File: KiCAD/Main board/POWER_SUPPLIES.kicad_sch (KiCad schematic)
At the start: 32 parts, among them U18 12V, U19 5V, U20 8V, U21 15V, U23 LIN_REG_±5V, U24 LIN_REG_±12V, U28 12V, U29 AP2111H-3.3TRG1, U31 AP2111H-3.3TRG1, U9 SEPIC_-15V_LT3579

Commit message: Main board
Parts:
- added TP17: TestPoint, TestPoint:TestPoint_Pad_D2.0mm, symbol Connector:TestPoint
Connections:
- net -15VD1: now reaches U23.6 (-VIN), U23.6 (-VIN), U24.6 (-VIN), U24.6 (-VIN), U9.3 (VOUT)
- net -15VD1: now also TP17.1
- net +15VD1: now reaches TP11.1, U21.1 (VOUT), U24.1 (+VIN), U24.1 (+VIN)
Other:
- moved on the sheet: C2, TP10, TP15, TP16, TP2, TP3, TP4, TP5, TP6, TP7, TP8, U23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

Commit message: Worked on main board schematic
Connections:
- net +12VD1: now also U28.2 (VOUT)
- net +15VD1: now also U21.2 (VOUT)
- net +5VD1: now also U19.2 (VOUT)
- net DC_POWER_IN: now also U18.5 (VIN), U19.5 (VIN), U20.5 (VIN), U21.5 (VIN), U28.5 (VIN); no longer U18.3 (VIN), U19.3 (VIN), U20.3 (VIN), U21.3 (VIN), U28.3 (VIN)
- net GND: now also U18.3 (GND), U18.4 (GND), U19.3 (GND), U19.4 (GND), U20.3 (GND), U20.4 (GND), U21.3 (GND), U21.4 (GND), U28.3 (GND), U28.4 (GND); no longer U18.2 (GND), U19.2 (GND), U20.2 (GND), U21.2 (GND), U28.2 (GND)
- net at TP9.1, U20.1 (VOUT), U23.1 (+VIN)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: now also U20.2 (VOUT)
- net at TP12.1, U18.1 (VOUT), U9.1 (VIN): now also U18.2 (VOUT)
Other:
- moved on the sheet: C2, TP1, TP10, TP11, TP12, TP13, TP15, TP16, TP17, TP2, TP3, TP4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

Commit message: Ad good as finilized the main board schematic
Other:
- note removed: "Check all regulator symbols and footprints with someone else"
- title: (none) -> AUDIO-DSP_MAIN_BOARD
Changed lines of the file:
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@@
 (kicad_sch (version 20230121) (generator eeschema)
   (paper "A4")
+  (title_block
+    (title "AUDIO-DSP_MAIN_BOARD")
+    (rev "R01")
+  )
   (junction (at 125.73 173.99) (diameter 0) (color 0 0 0 0)
   )
@@
   )
   (rectangle (start 93.98 35.56) (end 147.32 191.77)
-    (stroke (width 0) (type dash))
+    (stroke (width 0) (type dash) (color 100 100 100 1))
     (fill (type none))
   )
   (rectangle (start 13.97 13.97) (end 92.71 163.83)
-    (stroke (width 0) (type dash))
+    (stroke (width 0) (type dash) (color 100 100 100 1))
     (fill (type none))
   )
-  (text "Check all regulator symbols and footprints with someone else"
-    (at 93.98 34.29 0)
-    (effects (font (size 1.27 1.27) (color 200 0 200 1)) (justify left bottom))
-  )
   (text "Add thermal pad to pin 4 for cooling" (at 116.84 189.23 0)

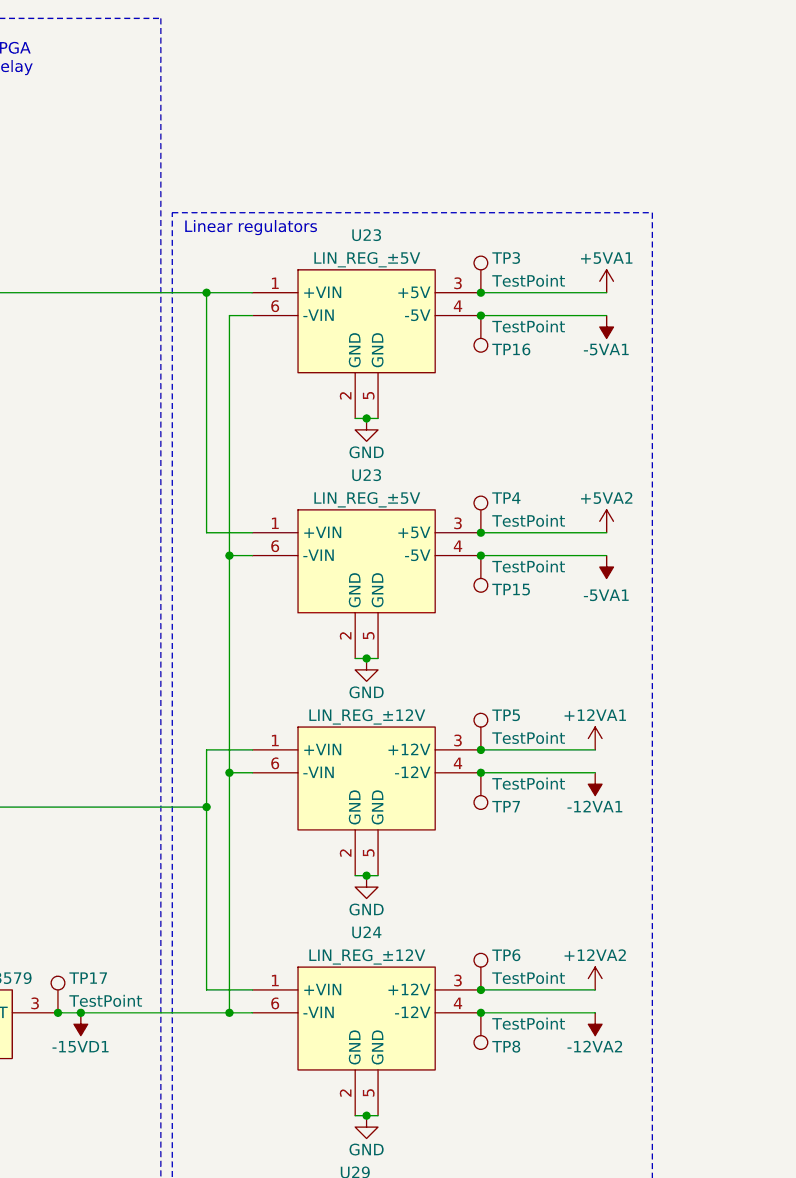
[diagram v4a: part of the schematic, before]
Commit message: Added component links to main board schematic
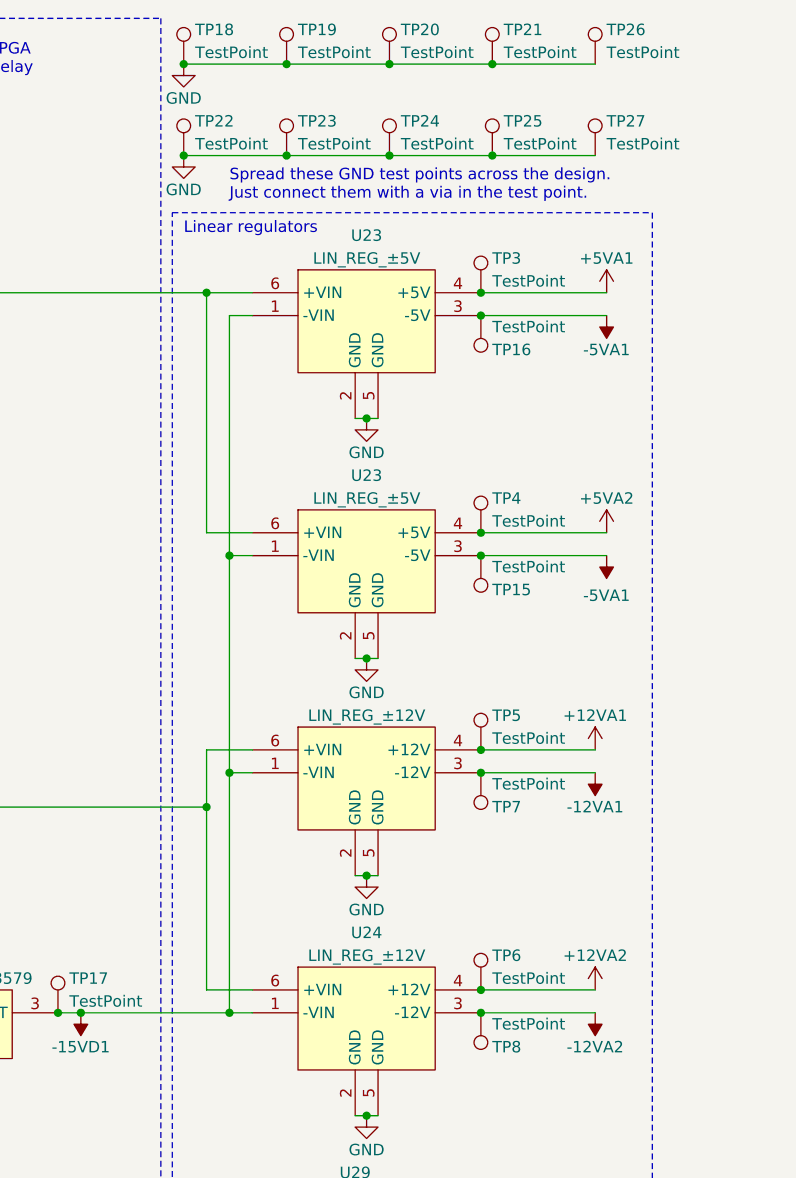
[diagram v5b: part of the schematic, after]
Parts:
- added TP18, TP19, TP20, TP21, TP22, TP23, TP24, TP25, TP26, TP27: TestPoint, TestPoint:TestPoint_Pad_D2.0mm, symbol Connector:TestPoint
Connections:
- net +12VA1: now also U24.4 (+12V); no longer U24.3 (+12V)
- net +12VA2: now also U24.4 (+12V); no longer U24.3 (+12V)
- net +15VD1: now also U24.6 (+VIN), U24.6 (+VIN); no longer U24.1 (+VIN), U24.1 (+VIN)
- net +5VA1: now also U23.4 (+5V); no longer U23.3 (+5V)
- net +5VA2: now also U23.4 (+5V); no longer U23.3 (+5V)
- net -12VA1: now also U24.3 (-12V); no longer U24.4 (-12V)
- net -12VA2: now also U24.3 (-12V); no longer U24.4 (-12V)
- net -15VD1: now also U23.1 (-VIN), U23.1 (-VIN), U24.1 (-VIN), U24.1 (-VIN); no longer U23.6 (-VIN), U23.6 (-VIN), U24.6 (-VIN), U24.6 (-VIN)
- net -5VA1: now also U23.3 (-5V), U23.3 (-5V); no longer U23.4 (-5V), U23.4 (-5V)
- net GND: now also TP18.1, TP19.1, TP20.1, TP21.1, TP22.1, TP23.1, TP24.1, TP25.1, TP26.1, TP27.1
- net at TP9.1, U20.1 (VOUT), U20.2 (VOUT): now also U23.6 (+VIN), U23.6 (+VIN); no longer U23.1 (+VIN), U23.1 (+VIN)
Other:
- note added: "Spread these GND test points across the design. Just connect them with a via in the test point."

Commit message: Main board
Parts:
- U23, U24: footprint Audio_DSP:LIN_REG_±xxV -> Audio-DSP:LIN_REG_±xxV
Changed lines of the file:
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@@
       (effects (font (size 1.27 1.27)))
     )
-    (property "Footprint" "Audio_DSP:LIN_REG_±xxV" (at 114.3 62.23 0)
+    (property "Footprint" "Audio-DSP:LIN_REG_±xxV" (at 114.3 62.23 0)
       (effects (font (size 1.27 1.27)) hide)
     )
@@
       (effects (font (size 1.27 1.27)))
     )
-    (property "Footprint" "Audio_DSP:LIN_REG_±xxV" (at 114.3 113.03 0)
+    (property "Footprint" "Audio-DSP:LIN_REG_±xxV" (at 114.3 113.03 0)
       (effects (font (size 1.27 1.27)) hide)
     )
@@
       (effects (font (size 1.27 1.27)))
     )
-    (property "Footprint" "Audio_DSP:LIN_REG_±xxV" (at 114.3 35.56 0)
+    (property "Footprint" "Audio-DSP:LIN_REG_±xxV" (at 114.3 35.56 0)
       (effects (font (size 1.27 1.27)) hide)
     )
@@
       (effects (font (size 1.27 1.27)))
     )
-    (property "Footprint" "Audio_DSP:LIN_REG_±xxV" (at 114.3 86.36 0)
-      (effects (font (size 1.27 1.27)) hide)
-    )
+    (property "Footprint" "Audio-DSP:LIN_REG_±xxV" (at 114.3 86.36 0)
+      (effects (font (size 1.27 1.27)) hide)
+    )

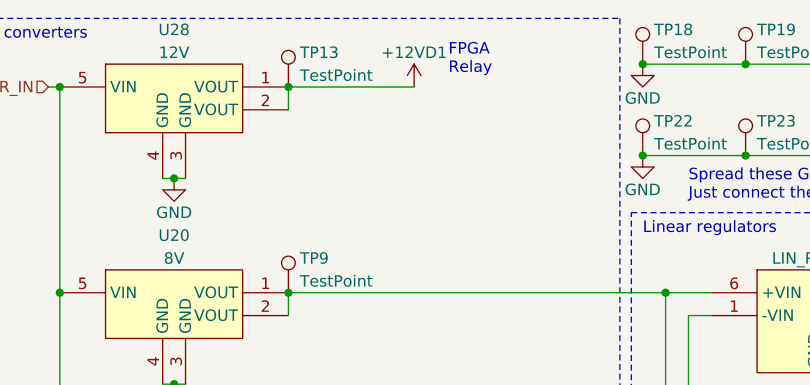
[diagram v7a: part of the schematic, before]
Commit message: Main board components to be ordered
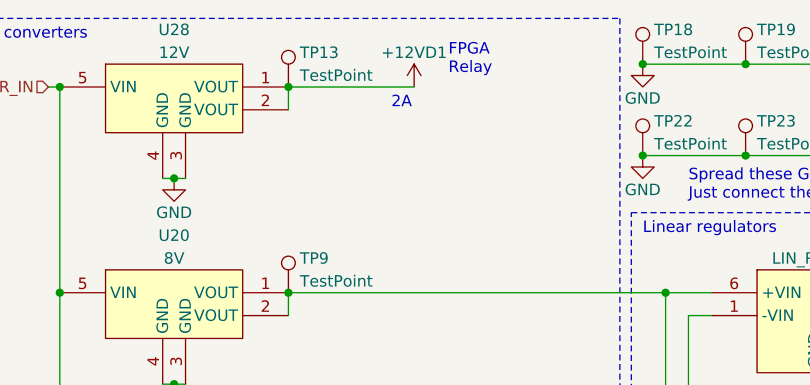
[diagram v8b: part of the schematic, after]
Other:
- note added: "2A"
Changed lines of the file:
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@@
+    (effects (font (size 1.27 1.27)) (justify left bottom))
+  )
+  (text "2A" (at 67.31 24.13 0)
     (effects (font (size 1.27 1.27)) (justify left bottom))
   )
